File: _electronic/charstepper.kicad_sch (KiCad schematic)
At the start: 8 parts

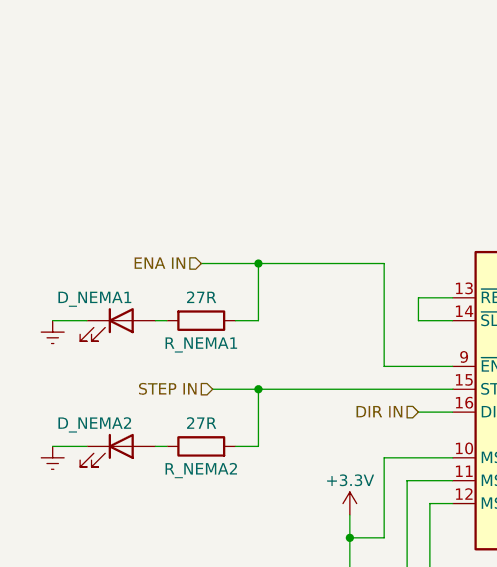
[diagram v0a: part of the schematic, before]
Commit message: revised pcb: direct power, leds, ftdi w/o 3v3
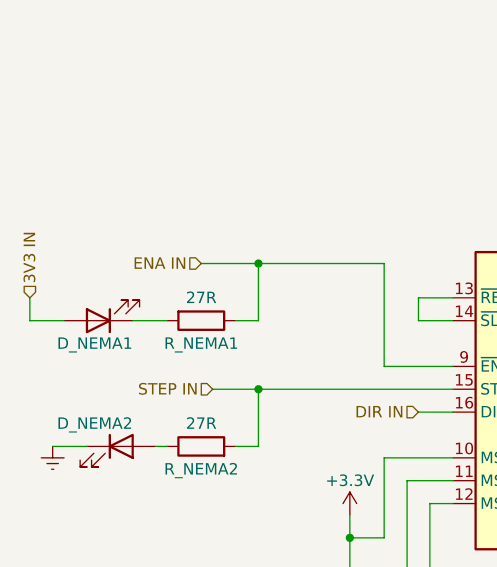
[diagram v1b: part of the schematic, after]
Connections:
- net 3V3 IN: now also D_NEMA1.2 (A)
- net GNDREF: no longer D_NEMA1.1 (K)
- net at R_NEMA1.2: now also D_NEMA1.1 (K); no longer D_NEMA1.2 (A)
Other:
- moved on the sheet: D_NEMA1
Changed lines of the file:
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@@
     (stroke (width 0) (type default) (color 0 0 0 0))
   )
-  (wire (pts (xy 105.41 96.52) (xy 106.68 96.52))
+  (wire (pts (xy 102.87 96.52) (xy 106.68 96.52))
     (stroke (width 0) (type default) (color 0 0 0 0))
   )
@@
     (stroke (width 0) (type default) (color 0 0 0 0))
   )
+  (wire (pts (xy 91.44 93.98) (xy 91.44 96.52))
+    (stroke (width 0) (type default) (color 0 0 0 0))
+  )
   (wire (pts (xy 204.47 93.98) (xy 204.47 97.79))
     (stroke (width 0) (type default) (color 0 0 0 0))
@@
     (stroke (width 0) (type default) (color 0 0 0 0))
   )
-  (wire (pts (xy 93.98 96.52) (xy 97.79 96.52))
+  (wire (pts (xy 91.44 96.52) (xy 95.25 96.52))
     (stroke (width 0) (type default) (color 0 0 0 0))
   )
@@
   )
   (hierarchical_label "3V3 IN" (shape input) (at 204.47 82.55 90)
+    (effects (font (size 1.27 1.27)) (justify left))
+  )
+  (hierarchical_label "3V3 IN" (shape input) (at 91.44 93.98 90)
     (effects (font (size 1.27 1.27)) (justify left))
   )
@@
     )
     (property "Datasheet" "" (id 3) (at 127 118.11 0)
-      (effects (font (size 1.27 1.27)) hide)
-    )
-    (pin "1")
-  )
-  (symbol (lib_id "power:GNDREF") (at 93.98 96.52 0) (unit 1)
-    (in_bom yes) (on_board yes) (fields_autoplaced)
-    (property "Reference" "#PWR0193" (id 0) (at 93.98 102.87 0)
-      (effects (font (size 1.27 1.27)) hide)
-    )
-    (property "Value" "GNDREF" (id 1) (at 93.98 101.6 0)
-      (effects (font (size 1.27 1.27)) hide)
-    )
-    (property "Footprint" "" (id 2) (at 93.98 96.52 0)
-      (effects (font (size 1.27 1.27)) hide)
-    )
-    (property "Datasheet" "" (id 3) (at 93.98 96.52 0)
       (effects (font (size 1.27 1.27)) hide)
     )
@@
     (pin "9")
   )
-  (symbol (lib_id "Device:LED") (at 101.6 96.52 0) (unit 1)
-    (in_bom yes) (on_board yes)
-    (property "Reference" "D_NEMA1" (id 0) (at 102.87 93.98 0)
-      (effects (font (size 1.27 1.27)) (justify right))
-    )
-    (property "Value" "LED white" (id 1) (at 99.06 101.6 0)
+  (symbol (lib_id "Device:LED") (at 99.06 96.52 180) (unit 1)
+    (in_bom yes) (on_board yes)
+    (property "Reference" "D_NEMA1" (id 0) (at 102.87 99.06 0)
+      (effects (font (size 1.27 1.27)) (justify left))
+    )
+    (property "Value" "LED white" (id 1) (at 101.6 91.44 0)
       (effects (font (size 1.27 1.27)) (justify left) hide)
     )
-    (property "Footprint" "LED_SMD:LED_0603_1608Metric_Pad1.05x0.95mm_HandSolder" (id 2) (at 101.6 96.52 0)
-      (effects (font (size 1.27 1.27)) hide)
-    )
-    (property "Datasheet" "https://br.mouser.com/datasheet/2/348/smld12-e-1874545.pdf" (id 3) (at 101.6 96.52 0)
-      (effects (font (size 1.27 1.27)) hide)
-    )
-    (property "#" "SMLD12WBN1W1" (id 4) (at 100.33 93.98 0)
+    (property "Footprint" "LED_SMD:LED_0603_1608Metric_Pad1.05x0.95mm_HandSolder" (id 2) (at 99.06 96.52 0)
+      (effects (font (size 1.27 1.27)) hide)
+    )
+    (property "Datasheet" "https://br.mouser.com/datasheet/2/348/smld12-e-1874545.pdf" (id 3) (at 99.06 96.52 0)
+      (effects (font (size 1.27 1.27)) hide)
+    )
+    (property "#" "SMLD12WBN1W1" (id 4) (at 100.33 99.06 0)
       (effects (font (size 1.27 1.27) italic) (justify left) hide)
     )
-    (property "Description" "Signal LED" (id 5) (at 101.6 96.52 0)
-      (effects (font (size 1.27 1.27)) hide)
-    )
-    (property "Group" "NEMA" (id 6) (at 101.6 96.52 0)
-      (effects (font (size 1.27 1.27)) hide)
-    )
-    (property "Mouser" "OK" (id 7) (at 101.6 96.52 0)
-      (effects (font (size 1.27 1.27)) hide)
-    )
+    (property "Description" "Signal LED" (id 5) (at 99.06 96.52 0)
+      (effects (font (size 1.27 1.27)) hide)
+    )
+    (property "Group" "NEMA" (id 6) (at 99.06 96.52 0)
+      (effects (font (size 1.27 1.27)) hide)
+    )
+    (property "Mouser" "OK" (id 7) (at 99.06 96.52 0)
+      (effects (font (size 1.27 1.27)) hide)
+    )

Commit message: v1 pcb
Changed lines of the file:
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@@
     (stroke (width 0) (type default) (color 0 0 0 0))
   )
-  (wire (pts (xy 97.79 110.49) (xy 93.98 110.49))
+  (wire (pts (xy 97.79 110.49) (xy 91.44 110.49))
     (stroke (width 0) (type default) (color 0 0 0 0))
   )
   (wire (pts (xy 91.44 93.98) (xy 91.44 96.52))
+    (stroke (width 0) (type default) (color 0 0 0 0))
+  )
+  (wire (pts (xy 91.44 110.49) (xy 91.44 113.03))
     (stroke (width 0) (type default) (color 0 0 0 0))
   )
@@
     (pin "2")
   )
+  (symbol (lib_id "power:GNDREF") (at 91.44 113.03 0) (unit 1)
+    (in_bom yes) (on_board yes) (fields_autoplaced)
+    (property "Reference" "#PWR0129" (id 0) (at 91.44 119.38 0)
+      (effects (font (size 1.27 1.27)) hide)
+    )
+    (property "Value" "GNDREF" (id 1) (at 91.44 118.11 0)
+      (effects (font (size 1.27 1.27)) hide)
+    )
+    (property "Footprint" "" (id 2) (at 91.44 113.03 0)
+      (effects (font (size 1.27 1.27)) hide)
+    )
+    (property "Datasheet" "" (id 3) (at 91.44 113.03 0)
+      (effects (font (size 1.27 1.27)) hide)
+    )
+    (pin "1")
+  )
   (symbol (lib_id "Device:C_Polarized") (at 182.88 90.17 0) (unit 1)
     (in_bom yes) (on_board yes)
@@
       (effects (font (size 1.27 1.27)) hide)
     )
-    (pin "1")
-  )
-  (symbol (lib_id "power:GNDREF") (at 93.98 110.49 0) (unit 1)
-    (in_bom yes) (on_board yes) (fields_autoplaced)
-    (property "Reference" "#PWR0194" (id 0) (at 93.98 116.84 0)
-      (effects (font (size 1.27 1.27)) hide)
-    )
-    (property "Value" "GNDREF" (id 1) (at 93.98 115.57 0)
-      (effects (font (size 1.27 1.27)) hide)
-    )
-    (property "Footprint" "" (id 2) (at 93.98 110.49 0)
-      (effects (font (size 1.27 1.27)) hide)
-    )
-    (property "Datasheet" "" (id 3) (at 93.98 110.49 0)
-      (effects (font (size 1.27 1.27)) hide)
-    )

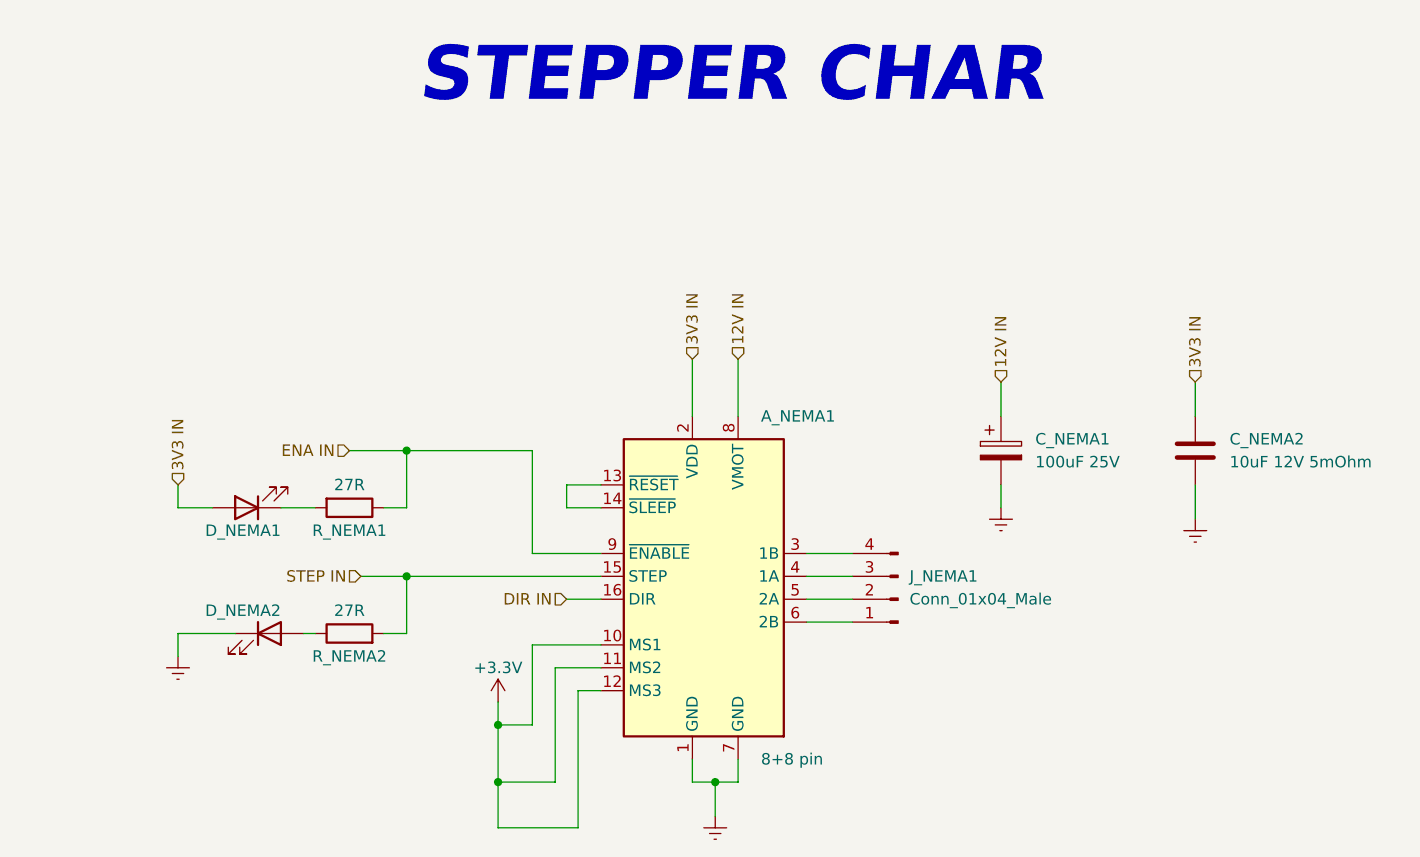
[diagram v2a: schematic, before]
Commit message: led resistor revision, b.o.m. and pcb anotation
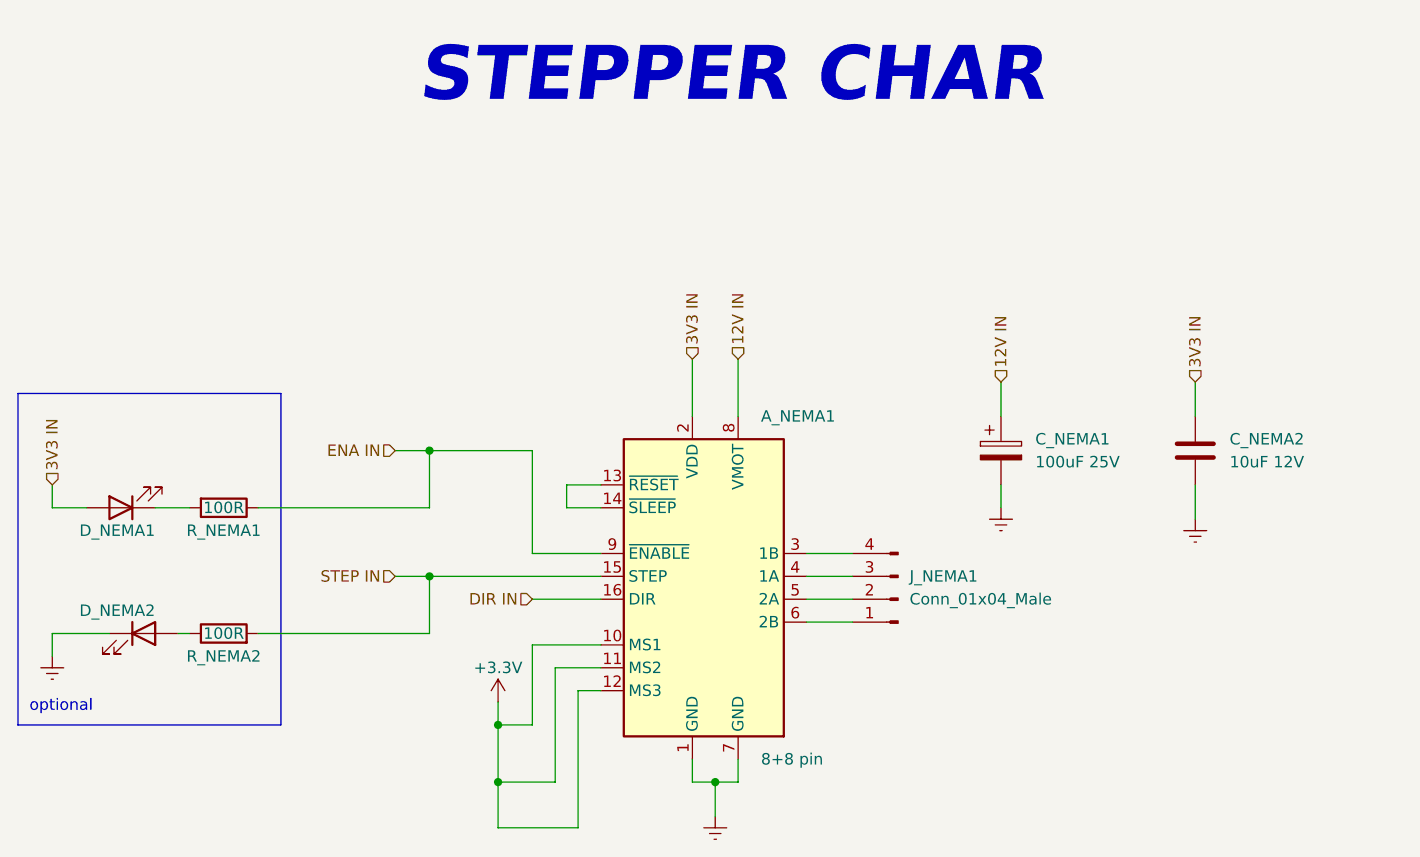
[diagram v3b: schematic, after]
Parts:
- C_NEMA2: value 10uF 12V 5mOhm -> 10uF 12V; # C1608X5R1E106M080AC -> GRM188Z71A106KA73D
- R_NEMA1, R_NEMA2: value 27R -> 100R; # CMP0603-FX-27R0ELF -> ERJ-3EKF1000V
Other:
- note added: "optional"
- moved on the sheet: D_NEMA1, D_NEMA2, R_NEMA1, R_NEMA2

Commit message: schematics and pcb cleanup
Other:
- note added: "optional LED feedback"
- note removed: "optional"
- title: E-TKT -> E-TKT v1.0
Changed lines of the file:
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@@
   (paper "A4")
   (title_block
-    (title "E-TKT")
-    (date "2022-07-21")
-    (rev "3")
+    (title "E-TKT v1.0")
+    (date "2022-09-29")
+    (rev "4")
     (company "Andrei Speridiao")
   )
@@
     (stroke (width 0) (type default) (color 0 0 0 0))
   )
-  (text "optional" (at 74.93 119.38 0)
+  (text "optional LED feedback" (at 74.93 119.38 0)
     (effects (font (size 1.27 1.27)) (justify left bottom))
   )
